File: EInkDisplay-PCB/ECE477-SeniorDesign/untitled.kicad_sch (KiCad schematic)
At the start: 0 parts

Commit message: push
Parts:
- added EinkDispCon1: ~, symbol EinkComponentLibrary:EinkDisplay
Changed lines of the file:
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@@
 	(generator_version "8.0")
 	(paper "A4")
+	(symbol
+		(lib_id "EinkComponentLibrary:EinkDisplay")
+		(at 129.54 115.57 0)
+		(unit 1)
+		(exclude_from_sim no)
+		(in_bom yes)
+		(on_board yes)
+		(dnp no)
+		(property "Reference" "EinkDispCon1"
+			(at 136.906 103.378 0)
+			(effects
+				(font
+					(size 1.27 1.27)
+				)
+			)
+		)
+		(property "Value" "~"
+			(at 135.89 102.87 0)
+			(effects
+				(font
+					(size 1.27 1.27)
+				)
+			)
+		)
+		(property "Footprint" ""
+			(at 135.89 87.63 0)
+			(effects
+				(font
+					(size 1.27 1.27)
+				)
+				(hide yes)
+			)
+		)
+		(property "Datasheet" ""
+			(at 135.89 87.63 0)
+			(effects
+				(font
+					(size 1.27 1.27)
+				)
+				(hide yes)
+			)
+		)
+		(property "Description" ""
+			(at 135.89 87.63 0)
+			(effects
+				(font
+					(size 1.27 1.27)
+				)
+				(hide yes)
+			)
+		)
+		(pin "1"
+		)
+		(pin "2"
+		)
+		(pin "7"
+		)
+		(pin "5"
+		)
+		(pin "6"
+		)
+		(pin "8"
+		)
+		(pin "4"
+		)
+		(pin "3"
+		)
+		(instances
+			(project "ECE477-SeniorDesign"
+				(path "/527ae649-08be-4368-9cf9-441ebba18eca/9aa04ce4-4558-41ab-8351-e46b80335092"
+					(reference "EinkDispCon1")
+					(unit 1)
+				)
+			)
+		)
+	)
 )

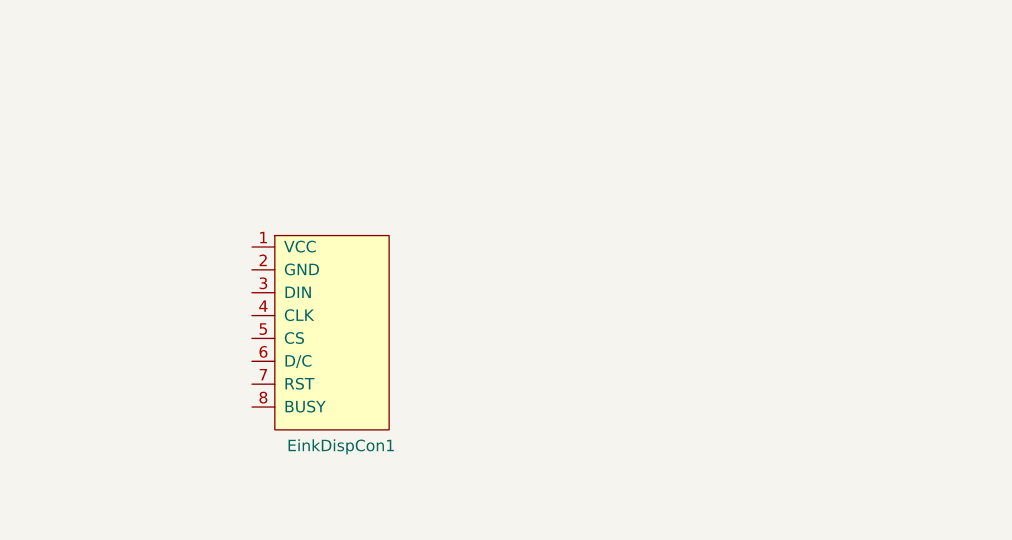
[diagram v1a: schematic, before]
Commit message: Adding SD
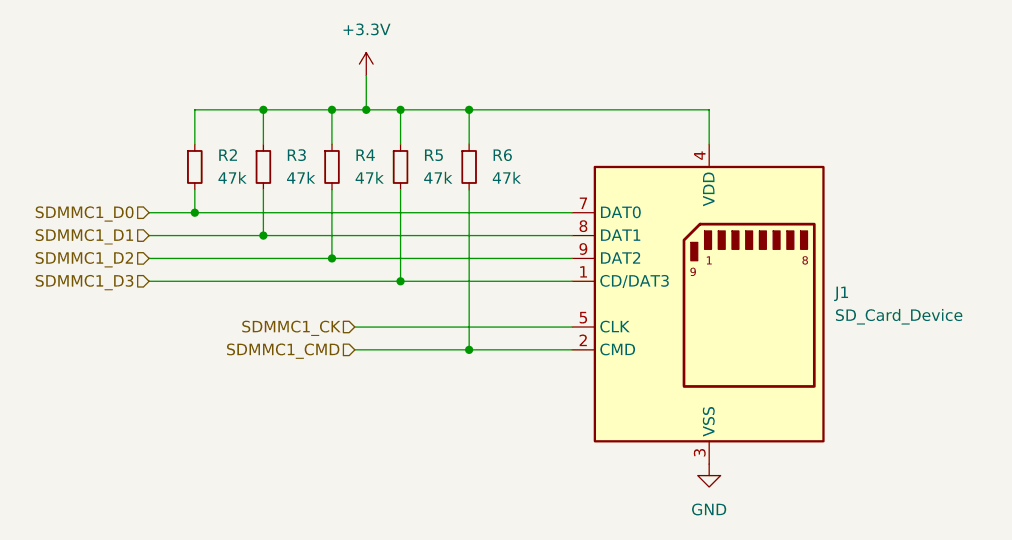
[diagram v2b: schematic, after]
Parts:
- removed EinkDispCon1: ~, symbol EinkComponentLibrary:EinkDisplay
- added J1: SD_Card_Device, symbol Connector:SD_Card_Device
- added R2, R3, R4, R5, R6: 47k, symbol Device:R_Small
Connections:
- new net +3.3V: J1.4 (VDD), R2.1, R3.1, R4.1, R5.1, R6.1
- new net GND: J1.3 (VSS), J1.6 (VSS)
- new net SDMMC1_CK: J1.5 (CLK)
- new net SDMMC1_CMD: J1.2 (CMD), R6.2
- new net SDMMC1_D0: J1.7 (DAT0), R2.2
- new net SDMMC1_D1: J1.8 (DAT1), R3.2
- new net SDMMC1_D2: J1.9 (DAT2), R4.2
- new net SDMMC1_D3: J1.1 (CD/DAT3), R5.2
